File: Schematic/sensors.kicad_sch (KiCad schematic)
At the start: 17 parts, among them IC4 ICM-42688-P, IC5 MPU-6500, U4 QMC5883L, U5 SPL06-001

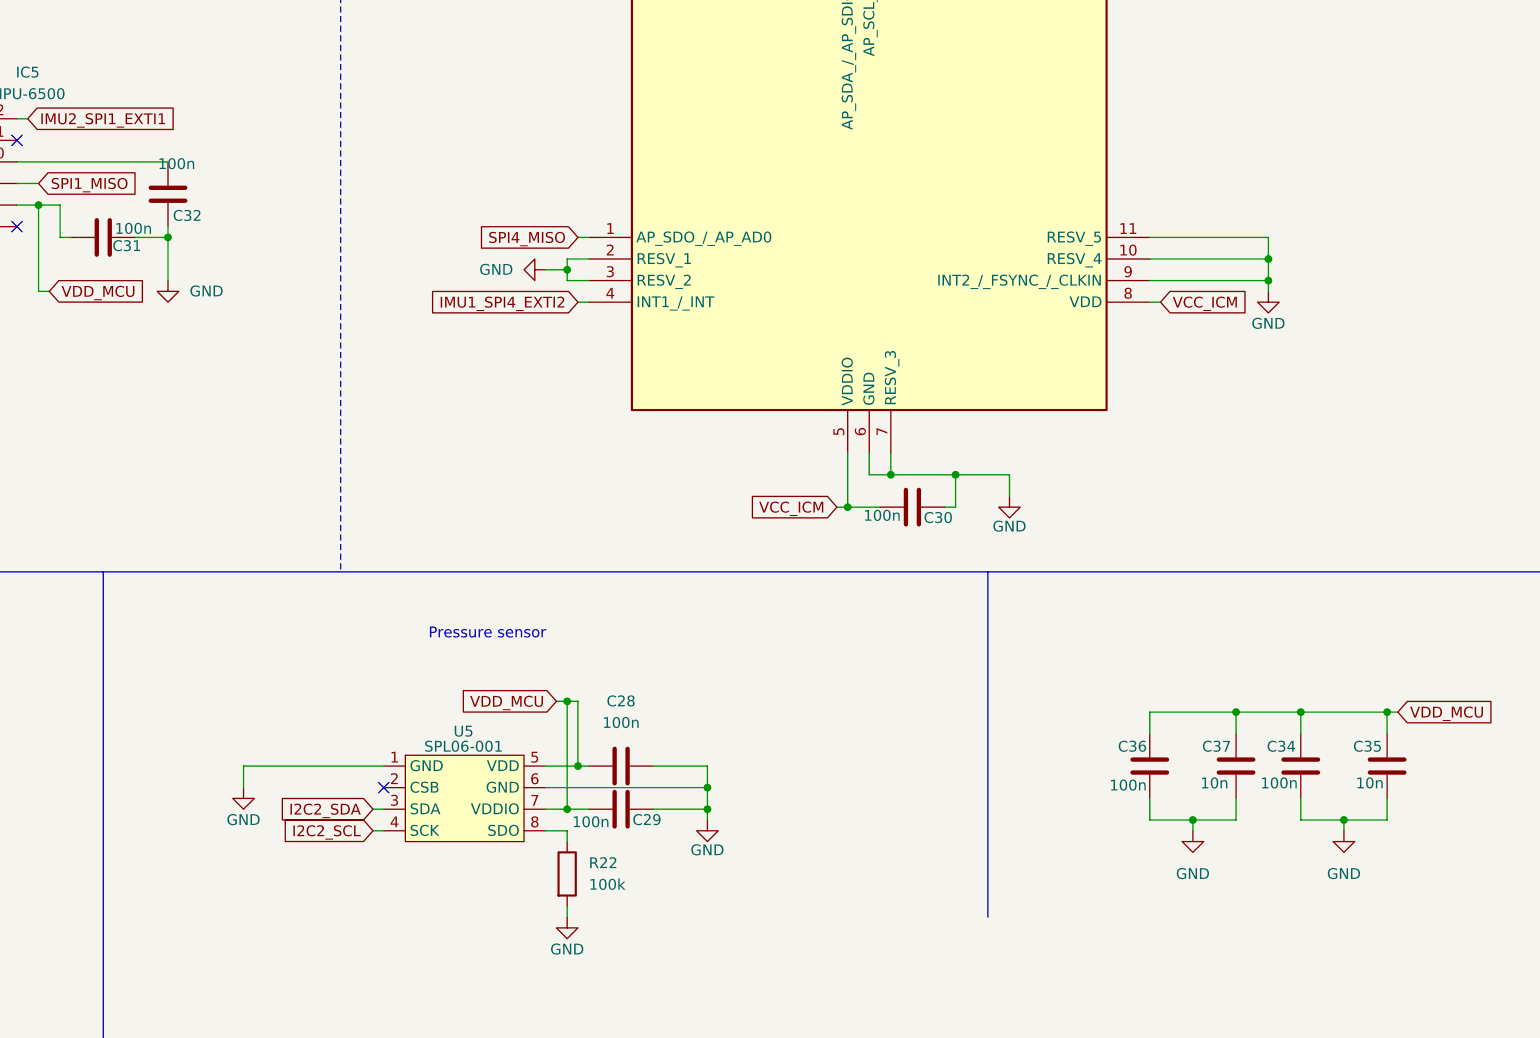
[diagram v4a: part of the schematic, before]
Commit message: update schematic after reviewing some footprints
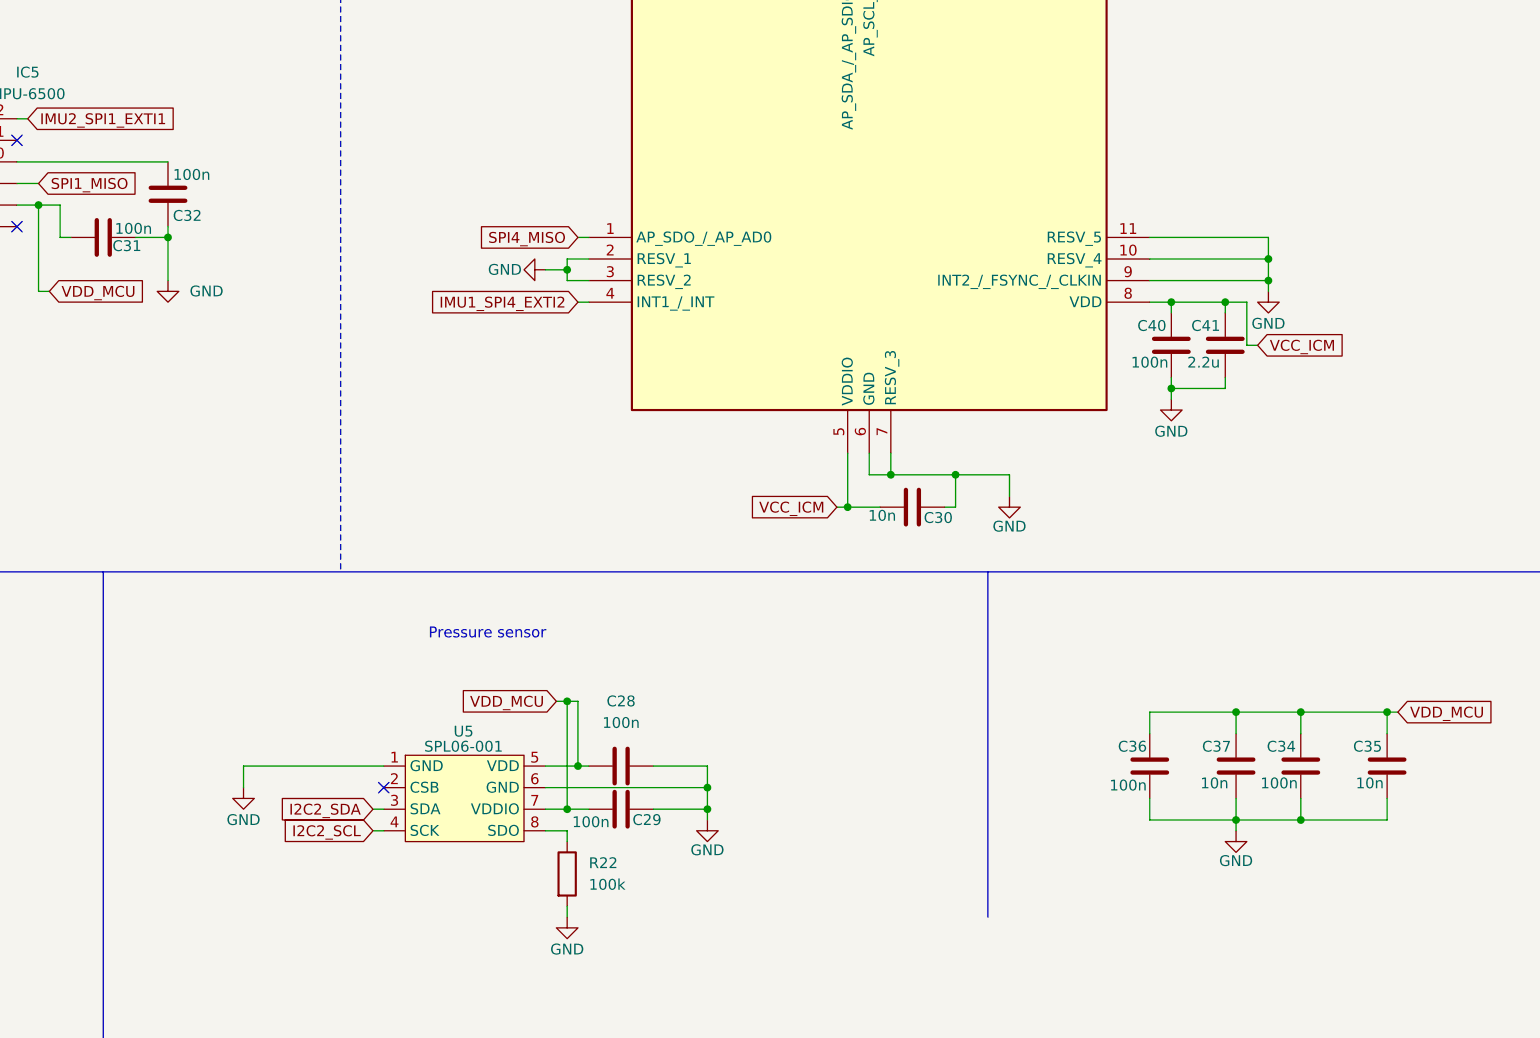
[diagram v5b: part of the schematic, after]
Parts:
- added C40: 100n, Capacitor_SMD:C_0603_1608Metric, symbol Device:C
- added C41: 2.2u, Capacitor_SMD:C_0603_1608Metric, symbol Device:C
- C28, C29, C31, C32, C33, C34, C36: MPN 0603B104K500NT -> (none); Manufacturer FH -> (none)
- C30: value 100n -> 10n; MPN 0603B104K500NT -> (none); Manufacturer FH -> (none)
- C35, C37: MPN CC0603KRX7R9BB103 -> (none); Manufacturer YAGEO -> (none)
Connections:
- net GND: now also C40.1, C41.1
- net VCC_ICM: now also C40.2, C41.2

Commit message: minor update and some checking
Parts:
- C28, C29, C31, C32, C33, C34, C36, C40: MPN (none) -> C0603X5R1E104K030BB; Manufacturer (none) -> TDK
- C30, C35, C37: MPN (none) -> TMK063B7103KP-F; Manufacturer (none) -> TAIYO YUDEN
- C41: MPN (none) -> 02016D225MAT2A; Manufacturer (none) -> KYOCERA AVX
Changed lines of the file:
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@@
 	(text "IMU1\n"
 		(exclude_from_sim no)
-		(at 72.898 44.958 0)
+		(at 72.898 47.244 0)
 		(effects
 			(font
@@
 			)
 		)
-		(property "Datasheet" ""
+		(property "Datasheet" "https://product.tdk.com/system/files/dam/doc/product/capacitor/ceramic/mlcc/catalog/mlcc_commercial_general_en.pdf?ref_disty=mouser"
 			(at 172.72 152.4 0)
 			(effects
@@
 			)
 		)
-		(property "MPN" ""
+		(property "MPN" "C0603X5R1E104K030BB"
 			(at 172.72 152.4 90)
 			(effects
@@
 			)
 		)
-		(property "Manufacturer" ""
+		(property "Manufacturer" "TDK"
 			(at 172.72 152.4 90)
 			(effects
@@
 			)
 		)
-		(property "Datasheet" ""
+		(property "Datasheet" "https://product.tdk.com/system/files/dam/doc/product/capacitor/ceramic/mlcc/catalog/mlcc_commercial_general_en.pdf?ref_disty=mouser"
 			(at 119.38 80.01 0)
 			(effects
@@
 			)
 		)
-		(property "MPN" ""
+		(property "MPN" "C0603X5R1E104K030BB"
 			(at 119.38 80.01 90)
 			(effects
@@
 			)
 		)
-		(property "Manufacturer" ""
+		(property "Manufacturer" "TDK"
 			(at 119.38 80.01 90)
 			(effects
@@
 			)
 		)
-		(property "Datasheet" ""
+		(property "Datasheet" "https://product.tdk.com/system/files/dam/doc/product/capacitor/ceramic/mlcc/catalog/mlcc_commercial_general_en.pdf?ref_disty=mouser"
 			(at 111.76 85.09 0)
 			(effects
@@
 			)
 		)
-		(property "MPN" ""
+		(property "MPN" "C0603X5R1E104K030BB"
 			(at 111.76 85.09 0)
 			(effects
@@
 			)
 		)
-		(property "Manufacturer" ""
+		(property "Manufacturer" "TDK"
 			(at 111.76 85.09 0)
 			(effects
@@
 			)
 		)
-		(property "Datasheet" ""
+		(property "Datasheet" "https://product.tdk.com/system/files/dam/doc/product/capacitor/ceramic/mlcc/catalog/mlcc_commercial_general_en.pdf?ref_disty=mouser"
 			(at 78.74 54.61 0)
 			(effects
@@
 			)
 		)
-		(property "MPN" ""
+		(property "MPN" "C0603X5R1E104K030BB"
 			(at 78.74 54.61 90)
 			(effects
@@
 			)
 		)
-		(property "Manufacturer" ""
+		(property "Manufacturer" "TDK"
 			(at 78.74 54.61 90)
 			(effects
@@
 			)
 		)
-		(property "Datasheet" ""
+		(property "Datasheet" "https://product.tdk.com/system/files/dam/doc/product/capacitor/ceramic/mlcc/catalog/mlcc_commercial_general_en.pdf?ref_disty=mouser"
 			(at 252.73 147.32 0)
 			(effects
@@
 			)
 		)
-		(property "MPN" ""
+		(property "MPN" "C0603X5R1E104K030BB"
 			(at 252.73 147.32 90)
 			(effects
@@
 			)
 		)
-		(property "Manufacturer" ""
+		(property "Manufacturer" "TDK"
 			(at 252.73 147.32 90)
 			(effects
@@
 			)
 		)
-		(property "Datasheet" ""
+		(property "Datasheet" "https://www.yuden.co.jp/productdata/catalog/mlcc02_e.pdf"
 			(at 207.01 116.84 0)
 			(effects
@@
 			)
 		)
-		(property "MPN" ""
+		(property "MPN" "TMK063B7103KP-F "
 			(at 207.01 116.84 90)
 			(effects
@@
 			)
 		)
-		(property "Manufacturer" ""
+		(property "Manufacturer" "TAIYO YUDEN"
 			(at 207.01 116.84 90)
 			(effects
@@
 			)
 		)
-		(property "Datasheet" ""
+		(property "Datasheet" "https://product.tdk.com/system/files/dam/doc/product/capacitor/ceramic/mlcc/catalog/mlcc_commercial_general_en.pdf?ref_disty=mouser"
 			(at 234.95 147.32 0)
 			(effects
@@
 			)
 		)
-		(property "MPN" ""
+		(property "MPN" "C0603X5R1E104K030BB"
 			(at 234.95 147.32 90)
 			(effects
@@
 			)
 		)
-		(property "Manufacturer" ""
+		(property "Manufacturer" "TDK"
 			(at 234.95 147.32 90)
 			(effects
@@
 			)
 		)
-		(property "Datasheet" ""
+		(property "Datasheet" "https://product.tdk.com/system/files/dam/doc/product/capacitor/ceramic/mlcc/catalog/mlcc_commercial_general_en.pdf?ref_disty=mouser"
 			(at 172.72 147.32 0)
 			(effects
@@
 			)
 		)
-		(property "MPN" ""
+		(property "MPN" "C0603X5R1E104K030BB"
 			(at 172.72 147.32 90)
 			(effects
@@
 			)
 		)
-		(property "Manufacturer" ""
+		(property "Manufacturer" "TDK"
 			(at 172.72 147.32 90)
 			(effects
@@
 		(on_board yes)
 		(dnp no)
-		(fields_autoplaced yes)
 		(property "Reference" "IC5"
-			(at 102.87 65.6746 90)
+			(at 90.17 62.484 90)
 			(effects
 				(font
@@
 		)
 		(property "Value" "MPU-6500"
-			(at 102.87 68.2146 90)
+			(at 90.424 64.77 90)
 			(effects
 				(font
@@
 			)
 		)
-		(property "Datasheet" ""
+		(property "Datasheet" "https://product.tdk.com/system/files/dam/doc/product/capacitor/ceramic/mlcc/catalog/mlcc_commercial_general_en.pdf?ref_disty=mouser"
 			(at 237.49 97.79 0)
 			(effects
@@
 			)
 		)
-		(property "MPN" ""
+		(property "MPN" "C0603X5R1E104K030BB"
 			(at 237.49 97.79 90)
 			(effects
@@
 			)
 		)
-		(property "Manufacturer" ""
+		(property "Manufacturer" "TDK"
 			(at 237.49 97.79 90)
 			(effects
@@
 			)
 		)
-		(property "Datasheet" ""
+		(property "Datasheet" "https://datasheets.kyocera-avx.com/cx5r-KGM.pdf"
 			(at 243.84 97.79 0)
 			(effects
@@
 			)
 		)
-		(property "MPN" ""
+		(property "MPN" "02016D225MAT2A"
 			(at 243.84 97.79 90)
 			(effects
@@
 			)
 		)
-		(property "Manufacturer" ""
+		(property "Manufacturer" "KYOCERA AVX"
 			(at 243.84 97.79 90)
 			(effects
@@
 			)
 		)
-		(property "Datasheet" ""
+		(property "Datasheet" "https://www.yuden.co.jp/productdata/catalog/mlcc02_e.pdf"
 			(at 245.11 147.32 0)
 			(effects
@@
 			)
 		)
-		(property "MPN" ""
+		(property "MPN" "TMK063B7103KP-F "
 			(at 245.11 147.32 90)
 			(effects
@@
 			)
 		)
-		(property "Manufacturer" ""
+		(property "Manufacturer" "TAIYO YUDEN"
 			(at 245.11 147.32 90)
 			(effects
@@
 			)
 		)
-		(property "Datasheet" ""
+		(property "Datasheet" "https://www.yuden.co.jp/productdata/catalog/mlcc02_e.pdf"
 			(at 262.89 147.32 0)
 			(effects
@@
 			)
 		)
-		(property "MPN" ""
+		(property "MPN" "TMK063B7103KP-F "
 			(at 262.89 147.32 90)
 			(effects
@@
 			)
 		)
-		(property "Manufacturer" ""
+		(property "Manufacturer" "TAIYO YUDEN"
 			(at 262.89 147.32 90)
 			(effects

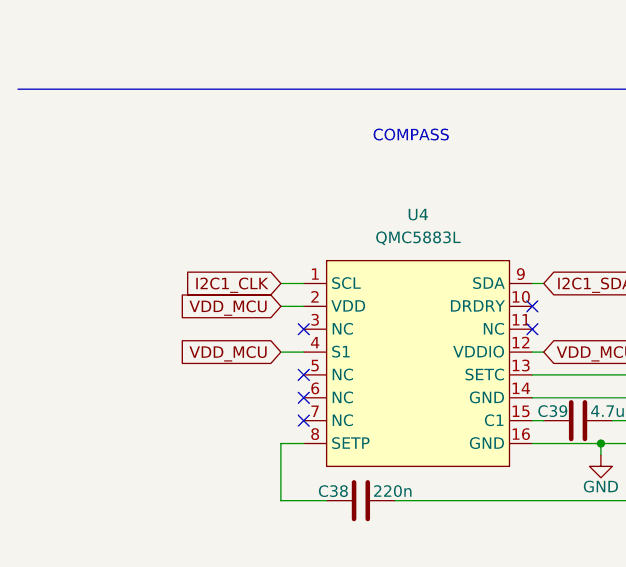
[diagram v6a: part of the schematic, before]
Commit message: optimisation : - refactoring two 4 pin connector for mag and gps into one 6 pin connector - increased output voltage from 5V buck regulator to take into account voltage decrease schottky diodes
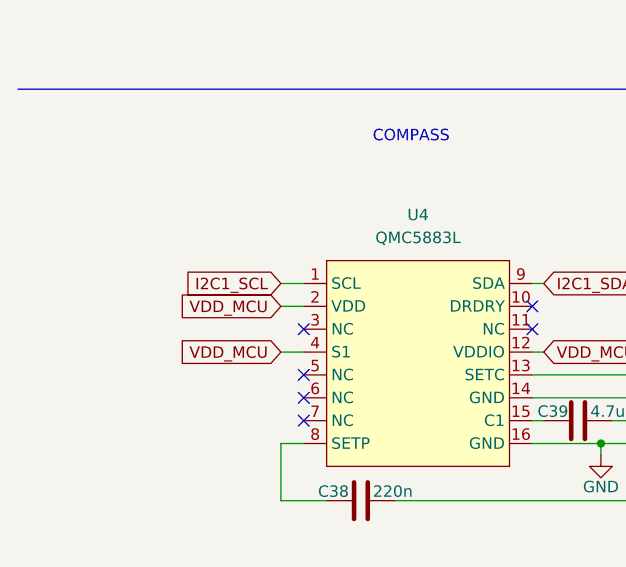
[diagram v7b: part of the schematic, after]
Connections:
- net I2C1_CLK renamed I2C1_SCL
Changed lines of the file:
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@@
 		)
 	)
-	(global_label "I2C1_CLK"
+	(global_label "I2C1_SCL"
 		(shape input)
 		(at 41.91 146.05 180)
@@
 		)
 		(property "Intersheetrefs" "${INTERSHEET_REFS}"
-			(at 30.0953 146.05 0)
+			(at 30.1558 146.05 0)
 			(effects
 				(font

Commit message: update on routing
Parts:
- C28, C29, C30, C31, C32, C33, C34, C35, C36, C37, C38, C39, C40, C41: footprint Capacitor_SMD:C_0603_1608Metric -> Capacitor_SMD:C_0402_1005Metric
- R22: footprint Resistor_SMD:R_0603_1608Metric -> Resistor_SMD:R_0402_1005Metric
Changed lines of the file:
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@@
 			)
 		)
-		(property "Footprint" "Capacitor_SMD:C_0603_1608Metric"
+		(property "Footprint" "Capacitor_SMD:C_0402_1005Metric"
 			(at 176.53 151.4348 0)
 			(effects
@@
 			)
 		)
-		(property "Footprint" "Capacitor_SMD:C_0603_1608Metric"
+		(property "Footprint" "Capacitor_SMD:C_0402_1005Metric"
 			(at 118.4148 76.2 0)
 			(effects
@@
 			)
 		)
-		(property "Footprint" "Capacitor_SMD:C_0603_1608Metric"
+		(property "Footprint" "Capacitor_SMD:C_0402_1005Metric"
 			(at 107.95 86.0552 0)
 			(effects
@@
 			)
 		)
-		(property "Footprint" "Capacitor_SMD:C_0603_1608Metric"
+		(property "Footprint" "Capacitor_SMD:C_0402_1005Metric"
 			(at 54.61 169.2148 0)
 			(effects
@@
 			)
 		)
-		(property "Footprint" "Capacitor_SMD:C_0603_1608Metric"
+		(property "Footprint" "Capacitor_SMD:C_0402_1005Metric"
 			(at 77.7748 50.8 0)
 			(effects
@@
 			)
 		)
-		(property "Footprint" "Capacitor_SMD:C_0603_1608Metric"
+		(property "Footprint" "Capacitor_SMD:C_0402_1005Metric"
 			(at 251.7648 143.51 0)
 			(effects
@@
 			)
 		)
-		(property "Footprint" "Capacitor_SMD:C_0603_1608Metric"
+		(property "Footprint" "Capacitor_SMD:C_0402_1005Metric"
 			(at 210.82 115.8748 0)
 			(effects
@@
 			)
 		)
-		(property "Footprint" "Capacitor_SMD:C_0603_1608Metric"
+		(property "Footprint" "Capacitor_SMD:C_0402_1005Metric"
 			(at 233.9848 143.51 0)
 			(effects
@@
 			)
 		)
-		(property "Footprint" "Capacitor_SMD:C_0603_1608Metric"
+		(property "Footprint" "Capacitor_SMD:C_0402_1005Metric"
 			(at 78.74 160.3248 0)
 			(effects
@@
 			)
 		)
-		(property "Footprint" "Capacitor_SMD:C_0603_1608Metric"
+		(property "Footprint" "Capacitor_SMD:C_0402_1005Metric"
 			(at 176.53 146.3548 0)
 			(effects
@@
 			)
 		)
-		(property "Footprint" "Capacitor_SMD:C_0603_1608Metric"
+		(property "Footprint" "Capacitor_SMD:C_0402_1005Metric"
 			(at 236.5248 93.98 0)
 			(effects
@@
 			)
 		)
-		(property "Footprint" "Capacitor_SMD:C_0603_1608Metric"
+		(property "Footprint" "Capacitor_SMD:C_0402_1005Metric"
 			(at 242.8748 93.98 0)
 			(effects
@@
 			)
 		)
-		(property "Footprint" "Capacitor_SMD:C_0603_1608Metric"
+		(property "Footprint" "Capacitor_SMD:C_0402_1005Metric"
 			(at 244.1448 143.51 0)
 			(effects
@@
 			)
 		)
-		(property "Footprint" "Resistor_SMD:R_0603_1608Metric"
+		(property "Footprint" "Resistor_SMD:R_0402_1005Metric"
 			(at 164.592 160.02 90)
 			(effects
@@
 			)
 		)
-		(property "Footprint" "Capacitor_SMD:C_0603_1608Metric"
+		(property "Footprint" "Capacitor_SMD:C_0402_1005Metric"
 			(at 261.9248 143.51 0)
 			(effects
